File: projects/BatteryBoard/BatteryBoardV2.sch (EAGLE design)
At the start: 187 parts, among them M1 BSO201SP, SW1 BTS50015-1TAD, SW2 BTS50015-1TAD, U1 LTC4412MPS6, U3 LTC4121-4.2, U4 LTC4121-4.2, U5 LTC4121, U6 LTC4121

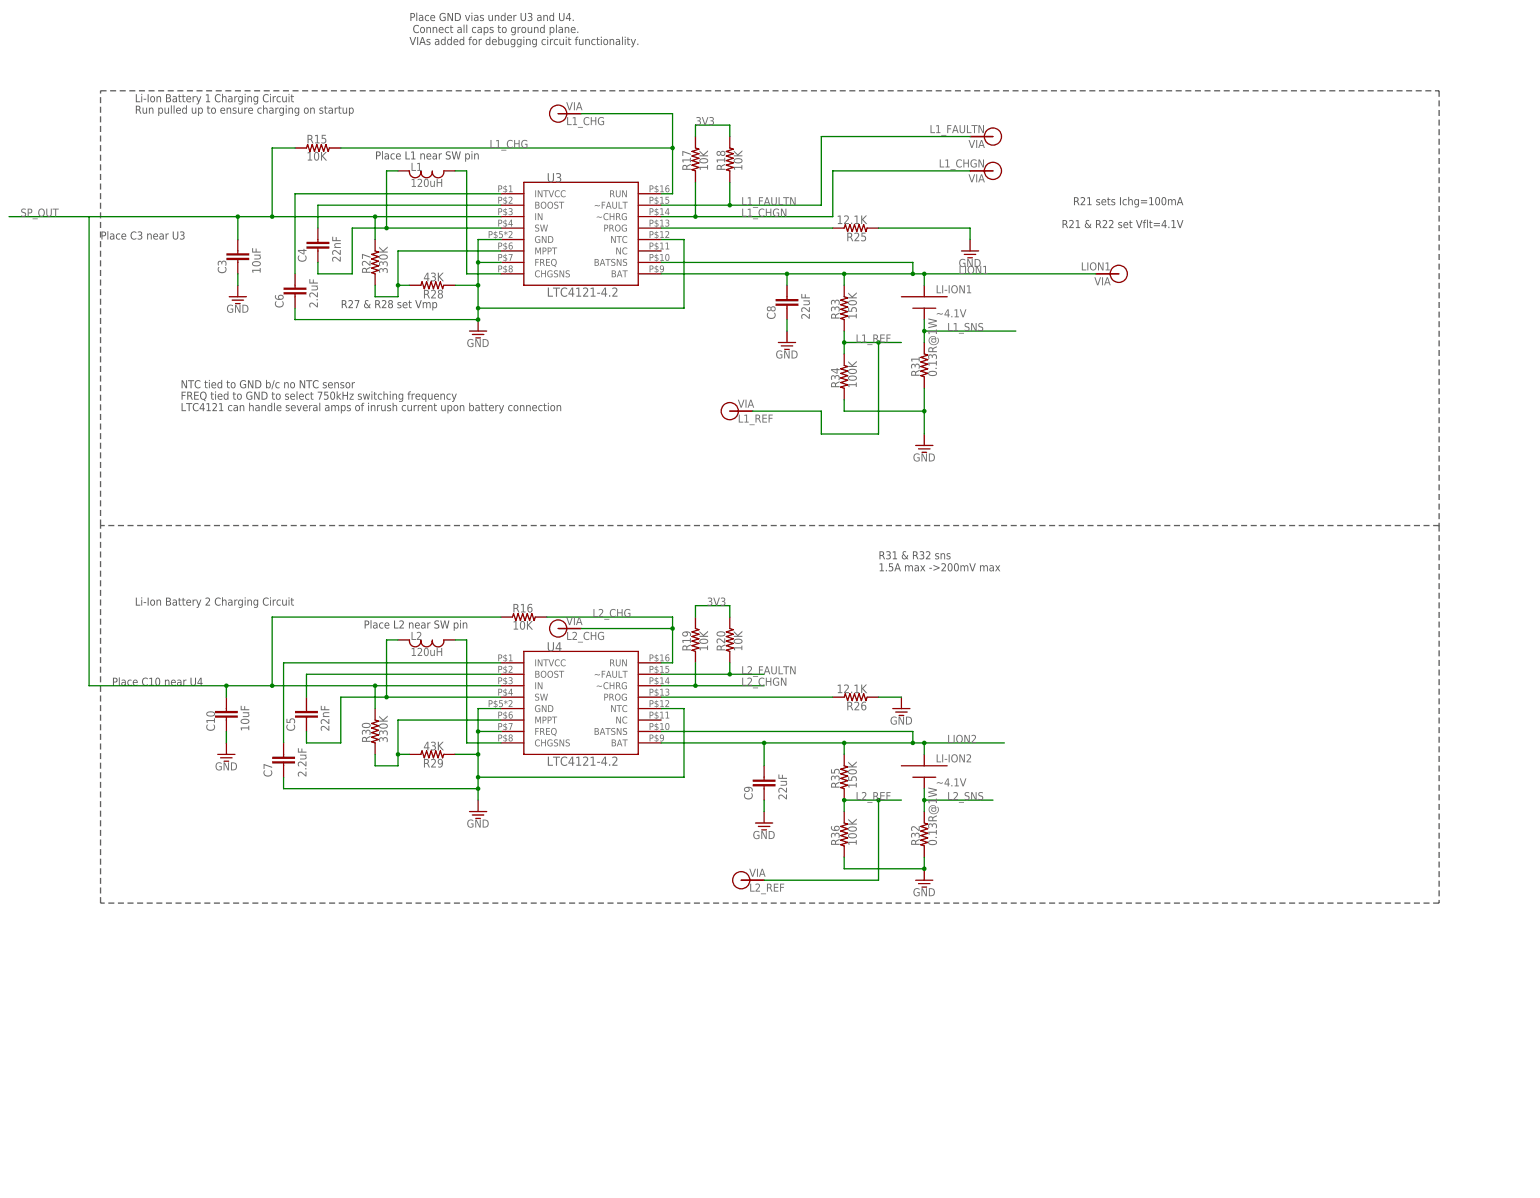
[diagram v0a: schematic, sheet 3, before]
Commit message: Finished programmer board and added output files to repo. Addiong of LDOs and continued fixes and updates to battery board v2.
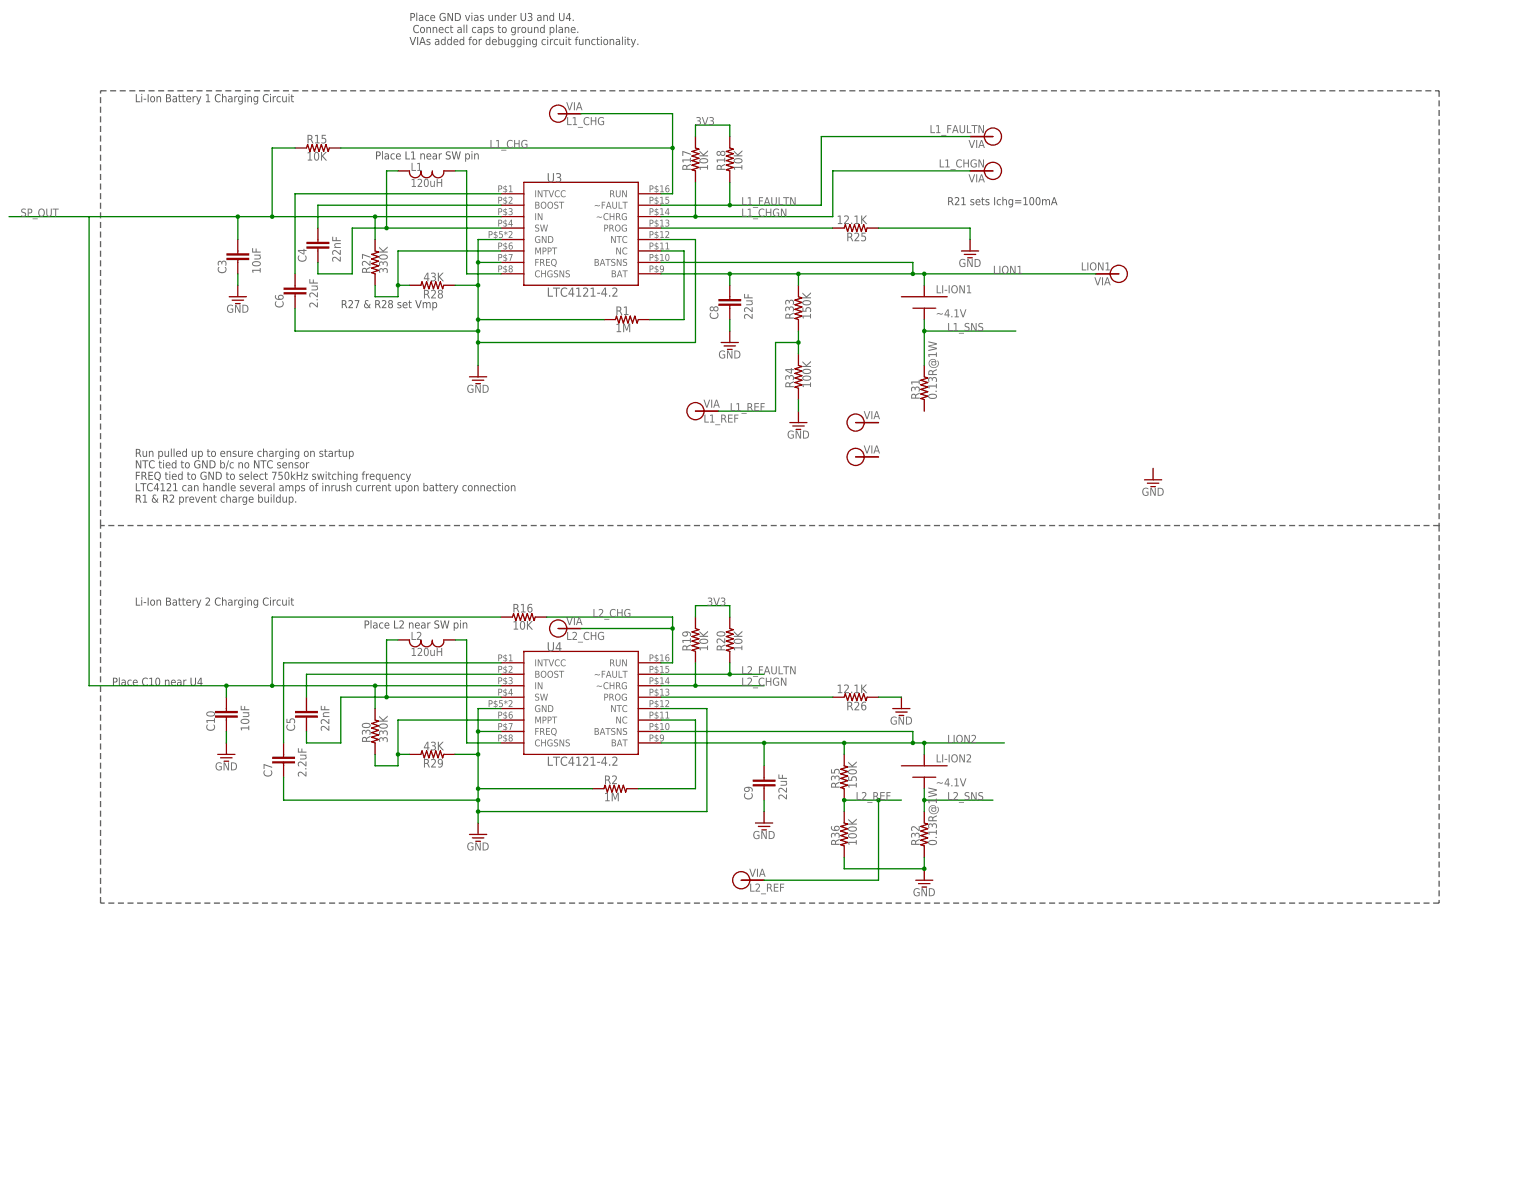
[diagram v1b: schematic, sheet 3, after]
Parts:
- removed R11: 10R, BrownSpaceEngineering:RES0805
- removed R12, R4: 0R, BrownSpaceEngineering:RES0805
- added C31, C34: 10uF, BrownSpaceEngineering:CAP0805
- added C32, C35: 0.01uF, BrownSpaceEngineering:CAP0805
- added C33, C36: 1uF, BrownSpaceEngineering:CAP0805
- added D2: DFLS130L, BrownSpaceEngineering:DFLS130L
- added R1: 1M, BrownSpaceEngineering:RES0805
- added U$7, U$8: LT1962-3, BrownSpaceEngineering:LT1962-3
- added V7, V8: (no value), BrownSpaceEngineering:VIA-60MIL
- D1: value (none) -> DFLS130L
- R2: value 0R -> 1M
- R84: value 1K -> 10K
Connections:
- removed net SP_C_O: R11.1, R12.1, R4.2, R5.2
- new net N$14: R2.2, U4.NC
- new net N$3: C34.P$1, C35.P$1, D2.A, U$8.OUT, U$8.SENSE
- new net N$4: C32.P$2, U$7.BYP
- new net N$6: R1.2, U3.NC
- net GND: now also C31.P$2, C33.P$2, C34.P$2, C36.P$2, R1.1, R2.1, U$7.GND, U$7.NC, U$8.GND, U$8.NC; no longer R31.1
- net L_OUT: now also D1.C, D2.C
- net N$2: now also C31.P$1, C32.P$1, D1.A, U$7.OUT, U$7.SENSE; no longer C2.P$1, M1.S, R4.1, U1.SNS
- net N$5: now also C35.P$2, U$8.BYP; no longer C1.P$1, M1.D, R2.2, U1.VIN
- net SP_C: now also C1.P$1, M1.D, U1.VIN; no longer R2.1
- net SP_OUT: now also C2.P$1, C33.P$1, C36.P$1, M1.S, R5.2, U$7.!SHDN!, U$7.IN, U$8.!SHDN!, U$8.IN, U1.SNS; no longer R11.2, R12.2
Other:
- note added: "Blocking diodes are on solar panels"
- note added: "Connect C32 directly to sense"
- note added: "Connect Sense to Out as closely as possible"
- note added: "LT1962-3: 3V output rated to 300mA"
- note added: "NC connected to ground is datasheet approved."
- note added: "R1 & R2 prevent charge buildup."
- note added: "SCL and SDA pull-ups are shared with ADC"
- note added: "Use large ground pours for GND and NC."
- note added: "XDL Receive Power <=0.5W. 0.5W/3V=167mA/2 =83mA ea. in parallel. From datasheet: P=Imax*(Vin-Vout) ::: P=0.583W -> 72.9C increase Tjmax = 125C -> 72.9C raise + 40C max temp gives Tj=112.9."
- note removed: "Current Sense Option"
- note removed: "R21 & R22 set Vflt=4.1V"
- note removed: "R31 & R32 sns 1.5A max ->200mV max"
- moved on the sheet: C8, D1, D6, R13, R14, R31, R33, R34

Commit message: Continued addition of changes to battery board v2. Small updates to library including some part descriptions.
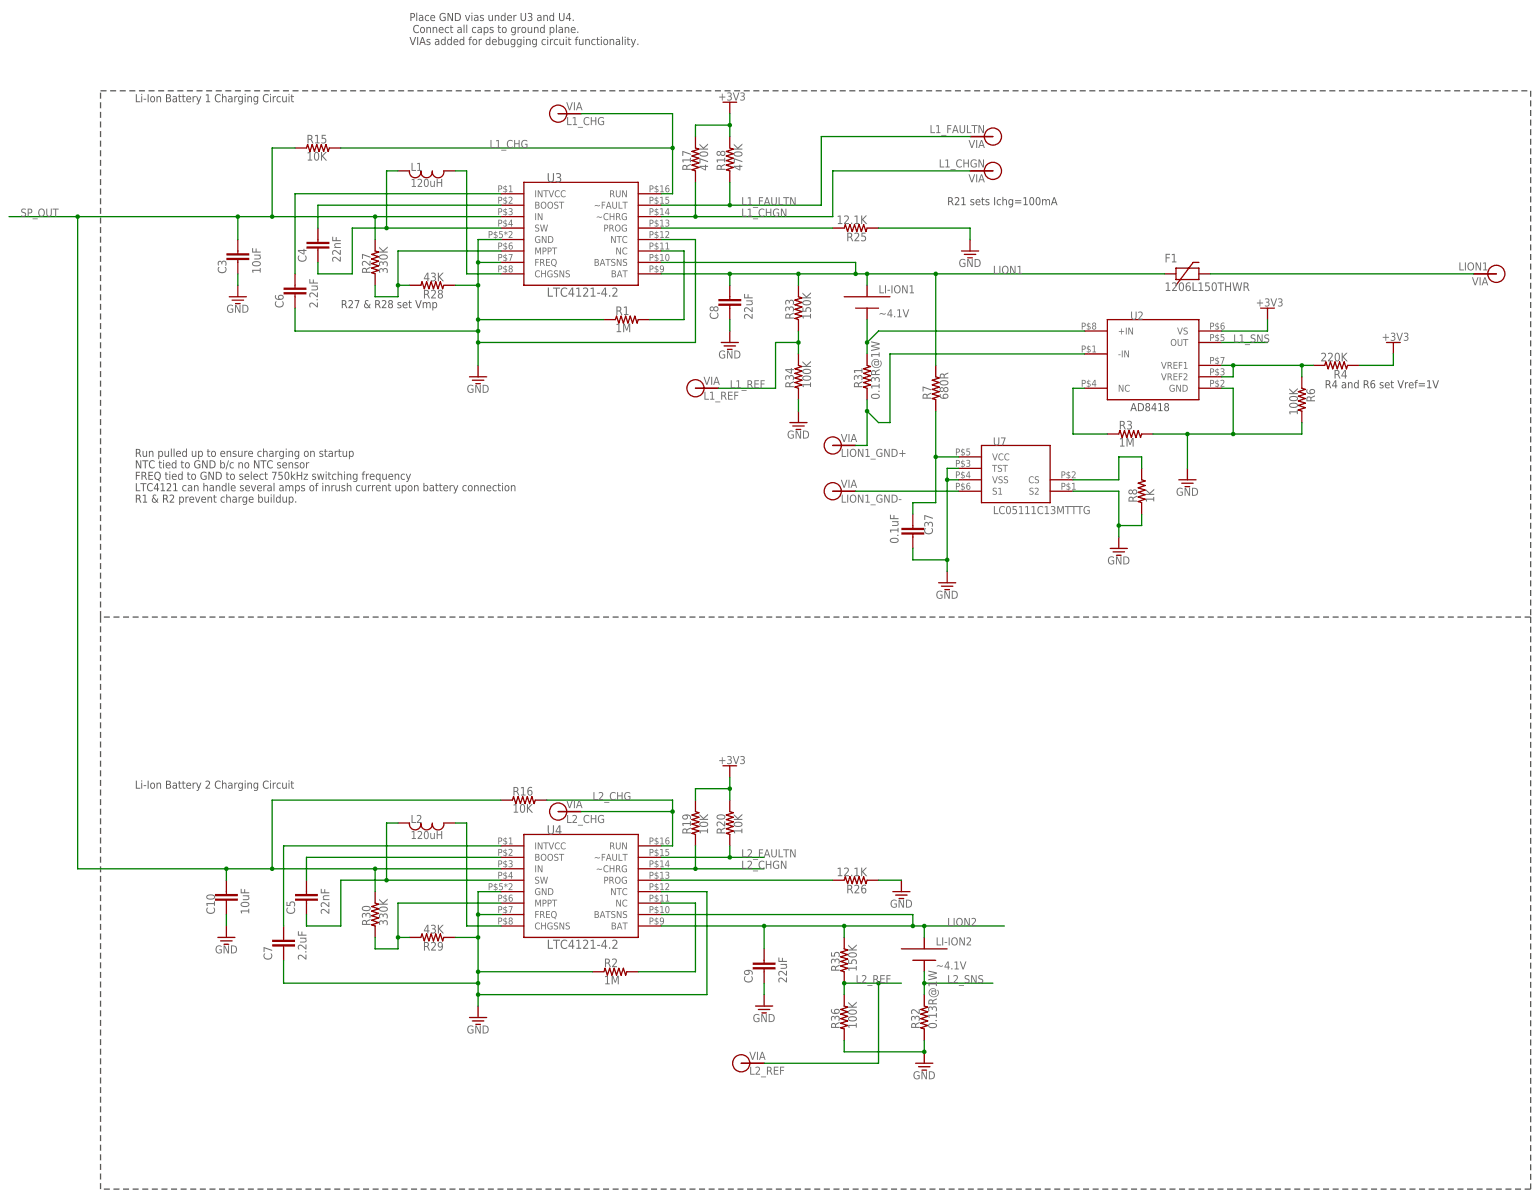
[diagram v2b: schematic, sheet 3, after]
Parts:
- added C37: 0.1uF, BrownSpaceEngineering:CAP0805
- added F1: 1206L150THWR, BrownSpaceEngineering:PTCFUSE1206
- added R3: 1M, BrownSpaceEngineering:RES0805
- added R4: 220K, BrownSpaceEngineering:RES0805
- added R6: 100K, BrownSpaceEngineering:RES0805
- added R7: 680R, BrownSpaceEngineering:RES0805
- added R8: 1K, BrownSpaceEngineering:RES0805
- added U2: AD8418, BrownSpaceEngineering:AD8418
- added U7: LC05111C13MTTTG, BrownSpaceEngineering:LC05111C13MTTTG
- R17, R18: value 10K -> 470K
- V7: value (none) -> LION1_GND+
- V8: value (none) -> LION1_GND-
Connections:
- removed net 3V3: C29.P$1, C30.P$1, R17.2, R18.2, R19.2, R20.2, R42.2, R43.2, R60.2, R61.2, R83.2, R84.2, R85.2, R86.2, U$4.VDD, U$6.VCC, V51.P$1
- new net +3V3: C29.P$1, C30.P$1, R17.2, R18.2, R19.2, R20.2, R4.1, R42.2, R43.2, R60.2, R61.2, R83.2, R84.2, R85.2, R86.2, U$4.VDD, U$6.VCC, U2.VS, V51.P$1
- new net L1_SNS+: LI-ION1.MINUS, R31.2, U2.+IN
- new net N$15: R31.1, U2.-IN, V7.P$1
- new net N$16: U7.S1, V8.P$1
- new net N$17: R3.1, U2.NC
- new net N$34: R4.2, R6.1, U2.VREF1, U2.VREF2
- new net N$44: C37.P$2, R7.1, U7.VCC
- new net N$45: R8.2, U7.CS
- new net N$46: F1.P$2, V45.P$1
- net GND: now also C37.P$1, R3.2, R6.2, R8.1, U2.GND, U7.S2, U7.TST, U7.VSS
- net L1_SNS: now also U2.OUT; no longer LI-ION1.MINUS, R31.2
- net LION1: now also F1.P$1, R7.2; no longer V45.P$1
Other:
- note added: "Connect +In and -In as close as possible to R31"
- note added: "R4 and R6 set Vref=1V"
- moved on the sheet: C10, C5, C7, C9, L2, LI-ION1, LI-ION2, R16, R19, R2, R20, R26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

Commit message: Continued improvements to the Battery Board schematic. Board reshaped.
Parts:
- removed D6: DFLS130L, BrownSpaceEngineering:DFLS130L
- removed R26: 12.1K, BrownSpaceEngineering:RES0805
- removed R29: 43K, BrownSpaceEngineering:RES0805
- removed R30: 330K, BrownSpaceEngineering:RES0805
- removed R32: 0.13R@1W, BrownSpaceEngineering:RES1210
- removed R35: 150K, BrownSpaceEngineering:RES0805
- removed R36: 100K, BrownSpaceEngineering:RES0805
- removed U$4: AD7991-0, BrownSpaceEngineering:AD7991-0
- removed U$6: TCA9535PWR, BrownSpaceEngineering:TCA9535PWR
- removed V54: L_OUT, BrownSpaceEngineering:VIA-120MIL
- removed V56: LF_B2_OUTEN, BrownSpaceEngineering:VIA-60MIL
- removed V58: LF1_REF, BrownSpaceEngineering:VIA-60MIL
- removed V59: LF2_REF, BrownSpaceEngineering:VIA-60MIL
- removed V61: LF4_REF, BrownSpaceEngineering:VIA-60MIL
- removed V62: LF3_REF, BrownSpaceEngineering:VIA-60MIL
- added C38: 10nF, BrownSpaceEngineering:CAP0805
- added D3: DFLS130L, BrownSpaceEngineering:DFLS130L
- added F2: 1206L200, BrownSpaceEngineering:PTCFUSE1206
- added R10: 330K, BrownSpaceEngineering:RES0805
- added R11: 43K, BrownSpaceEngineering:RES0805
- added R12: 0.13R@1W, BrownSpaceEngineering:RES1210
- added R21: 100K, BrownSpaceEngineering:RES0805
- added R22: 680R, BrownSpaceEngineering:RES0805
- added R23: 1K, BrownSpaceEngineering:RES0805
- added R9: 12.1K, BrownSpaceEngineering:RES0805
- added U14, U16: LTC4121, BrownSpaceEngineering:LTC4121
- added U8, U9: AD8418, BrownSpaceEngineering:AD8418
- added V11: LF3_TEMP, BrownSpaceEngineering:VIA-60MIL
- added V39: LIFE2, BrownSpaceEngineering:VIA60MIL-SQ
- added V40: LIFEB1SNS, BrownSpaceEngineering:VIA-60MIL
- added V43: LF_B1_OUTEN, BrownSpaceEngineering:VIA-60MIL
- added V44: LF_B1, BrownSpaceEngineering:VIA-120MIL
- added V46: LF_B1_OSNS, BrownSpaceEngineering:VIA-60MIL
- C10, C34: value 10uF -> 22nF
- C11, C12: value 4.7uF -> 22uF
- C13, C14: value 1uF -> 0.1uF
- C15: value 2.2uF -> 1uF
- C16: value 22nF -> 1uF
- C17: value 10uF -> 1uF
- C18: value 22uF -> 1uF
- C19: value 2.2uF -> 0.01uF
- C20: value 22nF -> 0.01uF
- C21: value 10uF -> 4.7uF
- C22: value 22uF -> 4.7uF
- C23, C24: value 10nF -> 10uF
- C25: value 150nF -> 10uF
- C26: value 10nF -> 2.2uF
- C27: value 10nF -> 22nF
- C28: value 150nF -> 22uF
- C29: value 0.1uF -> 150nF
- C3: value 10uF -> 0.1uF
- C30, C37: value 0.1uF -> 10nF
- C31: value 10uF -> 10nF
- C32: value 0.01uF -> 10uF
- C33: value 1uF -> 2.2uF
- C35: value 0.01uF -> 22uF
- C36: value 1uF -> 150nF
- C4: value 22nF -> 0.1uF
- C5: value 22nF -> 10uF
- C6: value 2.2uF -> 10uF
- C8: value 22uF -> 2.2uF
- C9: value 22uF -> 22nF
- F1: value 1206L150THWR -> 1206L200
- R1: value 1M -> 10K
- R16: value 10K -> 150K
- R19: value 10K -> 100K
- R2, R3: value 1M -> 470K
- R20: value 10K -> 220K
- U1: value LTC4412MPS6 -> TCA9535PWR; device BrownSpaceEngineering:LTC4412 -> BrownSpaceEngineering:TCA9535PWR
- U2: value AD8418 -> AD7991-0; device BrownSpaceEngineering:AD8418 -> BrownSpaceEngineering:AD7991-0
- U3: value LTC4121-4.2 -> LTC4412MPS6; device BrownSpaceEngineering:LTC4121-4.2 -> BrownSpaceEngineering:LTC4412
- U5: value LTC4121 -> LTC4121-4.2; device BrownSpaceEngineering:LTC4121 -> BrownSpaceEngineering:LTC4121-4.2
- U6: value LTC4121 -> LC05111C13MTTTG; device BrownSpaceEngineering:LTC4121 -> BrownSpaceEngineering:LC05111C13MTTTG
- V1: value UMB_CHG -> GND; device BrownSpaceEngineering:VIA-60MIL -> BrownSpaceEngineering:VIA-120MIL
- V10: value L1_CHG -> LF1_TEMP
- V12: value GND -> 3V3; device BrownSpaceEngineering:VIA60MIL-SQ -> BrownSpaceEngineering:VIA-60MIL
- V13: value GND -> X_P; device BrownSpaceEngineering:VIA-120MIL -> BrownSpaceEngineering:VIA-60MIL
- V14: value LIFEB1SNS -> X_P; device BrownSpaceEngineering:VIA-60MIL -> BrownSpaceEngineering:VIA60MIL-SQ
- V15: value LF_B1_CHG -> X_N
- V16: value LIFE2 -> Z_P; device BrownSpaceEngineering:VIA60MIL-SQ -> BrownSpaceEngineering:VIA-60MIL
- V17: value LIFE1 -> Z_N; device BrownSpaceEngineering:VIA60MIL-SQ -> BrownSpaceEngineering:VIA-60MIL
- V18: value LF_B1_CHGN -> Y_N
- V19: value LF_B1_FAULTN -> UMB_CHG
- V2: value X_P -> GND; device BrownSpaceEngineering:VIA-60MIL -> BrownSpaceEngineering:VIA-120MIL
- V20: value LF_B1_OUTEN -> L1_CHG
- V21: value LF_B1 -> L1_REF; device BrownSpaceEngineering:VIA-120MIL -> BrownSpaceEngineering:VIA-60MIL
- V22: value GND -> LION1_GND+; device BrownSpaceEngineering:VIA-120MIL -> BrownSpaceEngineering:VIA-60MIL
- V23: value GND -> LION1_GND-; device BrownSpaceEngineering:VIA-120MIL -> BrownSpaceEngineering:VIA-60MIL
- V24: value L1_TEMP -> LION2_GND+
- V25: value L1_REF -> LION2_GND-
- V26: value LF_B1 -> L1_FAULTN; device BrownSpaceEngineering:VIA-120MIL -> BrownSpaceEngineering:VIA60MIL-SQ
- V27: value LIFE_B2 -> L1_CHGN; device BrownSpaceEngineering:VIA-120MIL -> BrownSpaceEngineering:VIA60MIL-SQ
- V28: value LIFE_B2 -> LION1_OUT; device BrownSpaceEngineering:VIA-120MIL -> BrownSpaceEngineering:VIA60MIL-SQ
- V29: value L2_REF -> L1_DISG
- V3: value X_N -> GND; device BrownSpaceEngineering:VIA-60MIL -> BrownSpaceEngineering:VIA60MIL-SQ
- V30: value L_OUT -> L2_DISG; device BrownSpaceEngineering:VIA-120MIL -> BrownSpaceEngineering:VIA-60MIL
- V31: value LF_B1_OSNS -> L1_ST
- V32: value L2_TEMP -> L2_ST
- V33: value L2_CHG -> L_OUT; device BrownSpaceEngineering:VIA-60MIL -> BrownSpaceEngineering:VIA-120MIL
- V34: value L1_DISG -> L_OUT; device BrownSpaceEngineering:VIA-60MIL -> BrownSpaceEngineering:VIA-120MIL
- V35: value L2_DISG -> LF_B1_CHG
- V36: value L1_ST -> LF_B1_CHGN
- V37: value LF1_TEMP -> LF_B1_FAULTN
- V38: value L2_ST -> LIFE1; device BrownSpaceEngineering:VIA-60MIL -> BrownSpaceEngineering:VIA60MIL-SQ
- V4: value Z_P -> GND; device BrownSpaceEngineering:VIA-60MIL -> BrownSpaceEngineering:VIA-120MIL
- V41: value L1_FAULTN -> LF1_REF; device BrownSpaceEngineering:VIA60MIL-SQ -> BrownSpaceEngineering:VIA-60MIL
- V42: value L1_CHGN -> LF2_REF; device BrownSpaceEngineering:VIA60MIL-SQ -> BrownSpaceEngineering:VIA-60MIL
- V45: value LION1 -> LF_B1; device BrownSpaceEngineering:VIA60MIL-SQ -> BrownSpaceEngineering:VIA-120MIL
- V49: value X_P -> LF3_REF; device BrownSpaceEngineering:VIA60MIL-SQ -> BrownSpaceEngineering:VIA-60MIL
- V5: value Z_N -> SCL
- V50: value LF3_TEMP -> LF4_REF
- V51: value 3V3 -> LF_B2_OUTEN
- V52: value SCL -> LIFE_B2; device BrownSpaceEngineering:VIA-60MIL -> BrownSpaceEngineering:VIA-120MIL
- V53: value SDA -> LIFE_B2; device BrownSpaceEngineering:VIA-60MIL -> BrownSpaceEngineering:VIA-120MIL
- V6: value Y_N -> SDA
- V7: value LION1_GND+ -> 5V
- V8: value LION1_GND- -> L1_TEMP
- V9: value 5V -> L2_TEMP
- renumbered LIFE1TEMP to T3, LIFE3TEMP to T4, LIFEPO1 to LIFEPO41, LIFEPO2 to LIFEPO42, LIFEPO3 to LIFEPO43, LIFEPO4 to LIFEPO44, LION1TEMP to T1, LION2TEMP to T2, U$1 to U12, U$2 to U13, U$3 to U15, U$5 to U17, U$7 to U11, U$8 to U10, V57 to V47, V60 to V48, V63 to $6_188_$_2017-09-09_23-53-10
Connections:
- removed net N$10: C5.P$1, U4.BOOST
- removed net N$11: C5.P$2, L2.P$1, U4.SW
- removed net N$13 (its old number): C6.P$1, U3.INTVCC
- removed net N$15: R31.1, U2.-IN, V7.P$1
- removed net N$19: R25.2, U3.PROG
- removed net N$20: R26.2, U4.PROG
- removed net N$21: R29.2, R30.1, U4.MPPT
- removed net N$23: L2.P$2, U4.CHGSNS
- removed net N$46: F1.P$2, V45.P$1
- new net L1_PROG: R25.2, U4.PROG
- new net L1_SNS-: R31.1, U8.-IN, V22.P$1
- new net L2_PROG: R9.2, U5.PROG
- new net L2_SNS+: LI-ION2.MINUS, R12.2, U9.+IN
- new net L2_SNS-: R12.1, U9.-IN, V24.P$1
- new net LION1_OUT: C15.P$2, F1.P$2, U12.IN, V28.P$1
- new net LION2_OUT: C16.P$2, F2.P$2, U13.IN
- new net N$48: R10.1, R11.2, U5.MPPT
- new net N$49: L2.P$2, U5.CHGSNS
- new net N$51: R20.2, R21.1, U9.VREF1, U9.VREF2
- new net N$52: U7.S1, V25.P$1
- new net N$53: R23.2, U7.CS
- new net N$54: C14.P$2, R22.1, U7.VCC
- net !BATT_INT!: now also U1.!INT!; no longer U$6.!INT!
- net +3V3: now also C1.P$1, C2.P$1, R2.2, R20.1, R3.2, U1.VCC, U2.VDD, U8.VS, U9.VS, V12.P$1; no longer C29.P$1, C30.P$1, R19.2, R20.2, U$4.VDD, U$6.VCC, U2.VS, V51.P$1
- net 5V: now also V7.P$1; no longer V9.P$1
- net GND: now also C16.P$1, C17.P$2, C21.P$2, C26.P$1, C28.P$2, C29.P$1, C32.P$1, C33.P$1, C35.P$2, C36.P$1, C37.P$2, C38.P$2, C4.P$2, C5.P$2, R11.1, R19.1, R21.2, R23.1, R9.1, U1.A0, U1.A1, U1.A2, U14.FREQ, U14.GND, U14.NTC, U16.FREQ, U16.GND, U16.NTC, U3.CNTL, U4.NC, U5.NC, U6.S2, U6.TST, U6.VSS, U8.GND, U8.NC, U9.GND, U9.NC, V1.P$1, V2.P$1, V3.P$1, V4.P$1; no longer C10.P$2, C17.P$1, C19.P$1, C21.P$1, C26.P$2, C27.P$2, C28.P$1, C29.P$2, C33.P$2, C34.P$2, C36.P$2, C37.P$1, C9.P$2, R1.1, R2.1, R26.1, R29.1, R3.2, R32.1, R36.1, U$4.GND, U$6.A0, U$6.A1, U$6.A2, U$6.GND, U1.CNTL, U3.FREQ, U3.NTC, U6.FREQ, U6.GND, U6.NTC, V12.P$1, V13.P$1, V22.P$1, V23.P$1
- net L1_CHG: now also U4.RUN, V20.P$1; no longer U3.RUN, V10.P$1
- net L1_CHGN: now also U1.P04, U4.~CHRG, V27.P$1; no longer U$6.P04, U3.~CHRG, V42.P$1
- net L1_DISG: now also V29.P$1; no longer V34.P$1
- net L1_FAULTN: now also U1.P05, U4.~FAULT, V26.P$1; no longer U$6.P05, U3.~FAULT, V41.P$1
- net L1_REF: now also V21.P$1; no longer V25.P$1
- net L1_SNS: now also U2.VIN1, U8.OUT; no longer U$4.VIN1, U2.OUT
- net L1_SNS+: now also U8.+IN; no longer U2.+IN
- net L1_ST: now also U1.P01, V31.P$1; no longer U$6.P01, V36.P$1
- net L1_TEMP: now also V8.P$1; no longer V24.P$1
- net L2_CHG: now also R1.2, U5.RUN; no longer R16.2, U4.RUN, V33.P$1
- net L2_CHGN: now also R2.1, U1.P06, U5.~CHRG; no longer R19.1, U$6.P06, U4.~CHRG
- net L2_DISG: now also V30.P$1; no longer V35.P$1
- net L2_FAULTN: now also R3.1, U1.P07, U5.~FAULT; no longer R20.1, U$6.P07, U4.~FAULT
- net L2_REF: now also R16.1, R19.2; no longer R35.1, R36.2, V29.P$1
- net L2_SNS: now also U2.VIN0, U9.OUT; no longer LI-ION2.MINUS, R32.2, U$4.VIN0
- net L2_ST: now also U1.P00, V32.P$1; no longer U$6.P00, V38.P$1
- net L2_TEMP: now also V9.P$1; no longer V32.P$1
- net LF1_REF: now also V41.P$1; no longer V58.P$1
- net LF1_TEMP: now also V10.P$1; no longer V37.P$1
- net LF2_REF: now also V42.P$1; no longer V59.P$1
- net LF3_REF: now also V49.P$1; no longer V62.P$1
- net LF3_TEMP: now also V11.P$1; no longer V50.P$1
- net LF4_REF: now also V50.P$1; no longer V61.P$1
- net LF_B1: now also C30.P$1, V44.P$1, V45.P$1; no longer C23.P$1, V21.P$1, V26.P$1
- net LF_B1_BT: now also U1.P10; no longer U$6.P10
- net LF_B1_CHG: now also U14.RUN, V35.P$1; no longer U5.RUN, V15.P$1
- net LF_B1_CHGN: now also U1.P16, U14.~CHRG, V36.P$1; no longer U$6.P16, U5.~CHRG, V18.P$1
- net LF_B1_FAULTN: now also U1.P17, U14.~FAULT, V37.P$1; no longer U$6.P17, U5.~FAULT, V19.P$1
- net LF_B1_OSNS: now also C31.P$1, V46.P$1; no longer C24.P$1, V31.P$1
- net LF_B1_OUTEN: now also V43.P$1; no longer V20.P$1
- net LF_B1_TT: now also U1.P11; no longer U$6.P11
- net LF_B2_BT: now also U1.P13; no longer U$6.P13
- net LF_B2_CHG: now also U16.RUN; no longer U6.RUN
- net LF_B2_CHGN: now also U1.P14, U16.~CHRG; no longer U$6.P14, U6.~CHRG
- net LF_B2_FAULTN: now also U1.P15, U16.~FAULT; no longer U$6.P15, U6.~FAULT
- net LF_B2_OSNS: now also C38.P$1; no longer C27.P$1
- net LF_B2_OUTEN: now also V51.P$1; no longer V56.P$1
- net LF_B2_TT: now also U1.P12; no longer U$6.P12
- net LIFE1: now also C28.P$1, U14.BAT, V38.P$1; no longer C18.P$1, U5.BAT, V17.P$1
- net LIFE2: now also V39.P$1; no longer V16.P$1
- net LIFE3: now also C35.P$1, U16.BAT; no longer C22.P$1, U6.BAT
- net LIFEB1SNS: now also V40.P$1; no longer V14.P$1
- net LIFE_B2: now also C37.P$1, V52.P$1, V53.P$1; no longer C26.P$1, V27.P$1, V28.P$1
- net LION1: now also C11.P$1, U4.BAT, U4.BATSNS; no longer C13.P$2, C8.P$1, U12.IN, U3.BAT, U3.BATSNS
- net LION2: now also C12.P$1, F2.P$1, R16.2, R22.2, U5.BAT, U5.BATSNS; no longer C14.P$2, C9.P$1, R35.2, U13.IN, U4.BAT, U4.BATSNS
- net L_OUT: now also C21.P$1, C22.P$1, D3.C, V33.P$1, V34.P$1; no longer C11.P$1, C12.P$1, D1.C, V30.P$1, V54.P$1
- net L_REF: now also U2.VIN2; no longer U$4.VIN2
- net N$1: now also U3.GATE; no longer U1.GATE
- net N$1356: now also C36.P$2; no longer C28.P$2
- net N$14: now also C10.P$1, U5.BOOST; no longer R2.2, U4.NC
- net N$16: now also U6.S1, V23.P$1; no longer U7.S1, V8.P$1
- net N$17: now also C8.P$1, U5.INTVCC; no longer R3.1, U2.NC
- net N$18: now also U4.CHGSNS; no longer U3.CHGSNS
- net N$2: now also C20.P$1, C24.P$1, D3.A; no longer C31.P$1, C32.P$1, D1.A
- net N$22: now also U4.MPPT; no longer U3.MPPT
- net N$26: now also U14.FBG; no longer U5.FBG
- net N$27: now also U14.MPPT; no longer U5.MPPT
- net N$28: now also U14.FB; no longer U5.FB
- net N$29: now also C26.P$2, U14.INTVCC; no longer C15.P$2, U5.INTVCC
- net N$3: now also C19.P$1, C23.P$1; no longer C34.P$1, C35.P$1
- net N$30: now also C27.P$1, U14.SW; no longer C16.P$1, U5.SW
- net N$31: now also C27.P$2, U14.BOOST; no longer C16.P$2, U5.BOOST
- net N$32: now also U14.CHGSNS; no longer U5.CHGSNS
- net N$33: now also U16.MPPT; no longer U6.MPPT
- net N$34: now also U8.VREF1, U8.VREF2; no longer U2.VREF1, U2.VREF2
- net N$35: now also U16.PROG; no longer U6.PROG
- net N$36: now also U16.FBG; no longer U6.FBG
- net N$37: now also U16.FB; no longer U6.FB
- net N$38: now also C33.P$2, U16.INTVCC; no longer C19.P$2, U6.INTVCC
- net N$39: now also C34.P$1, U16.SW; no longer C20.P$1, U6.SW
- net N$4: now also C20.P$2; no longer C32.P$2
- net N$40: now also C34.P$2, U16.BOOST; no longer C20.P$2, U6.BOOST
- net N$41: now also U16.CHGSNS; no longer U6.CHGSNS
- net N$44: now also C13.P$2, U6.VCC; no longer C37.P$2, U7.VCC
- net N$45: now also U6.CS; no longer U7.CS
- net N$5: now also C19.P$2; no longer C35.P$2
- net N$6: now also C10.P$2, L2.P$1, U5.SW; no longer R1.2, U3.NC
- net N$68: now also C29.P$2; no longer C25.P$2
- net N$7: now also U14.PROG; no longer U5.PROG
- net N$8: now also C9.P$2, U4.SW; no longer C4.P$2, U3.SW
- net N$9: now also C9.P$1, U4.BOOST; no longer C4.P$1, U3.BOOST
- net PANELREF: now also U2.VIN3/REF; no longer U$4.VIN3/REF
- net SCL: now also U1.SCL, U2.SCL, V5.P$1; no longer U$4.SCL, U$6.SCL, V52.P$1
- net SDA: now also U1.SDA, U2.SDA, V6.P$1; no longer U$4.SDA, U$6.SDA, V53.P$1
- net SPF_ST: now also U1.P02, U3.STAT; no longer U$6.P02, U1.STAT
- net SP_C: now also C3.P$1, U3.VIN, V13.P$1, V14.P$1, V15.P$1, V16.P$1, V17.P$1, V18.P$1; no longer C1.P$1, U1.VIN, V2.P$1, V3.P$1, V4.P$1, V49.P$1, V5.P$1, V6.P$1
- net SP_OUT: now also C17.P$1, C18.P$1, C25.P$2, C32.P$2, C4.P$1, C5.P$1, C6.P$1, D1.C, R1.1, R10.2, U14.IN, U16.IN, U3.SNS; no longer C10.P$1, C17.P$2, C2.P$1, C21.P$2, C3.P$1, C33.P$1, C36.P$1, D6.C, R16.1, R30.2, U1.SNS, U3.IN, U6.IN
- net UMB_CHG: now also D1.A, V19.P$1; no longer D6.A, V1.P$1
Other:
- note added: "Connect +In and -In as close as possible to R12"
- note added: "NC tied to ground prevent charge buildup, approved by LT."
- note added: "NC tied to ground to prevent charge buildup, approved by AD."
- note added: "Place C5 near U4"
- note added: "R27 & R28 set Vmp=9V"
- note removed: "Place C10 near U4"
- note removed: "R1 & R2 prevent charge buildup."
- note removed: "R27 & R28 set Vmp"
